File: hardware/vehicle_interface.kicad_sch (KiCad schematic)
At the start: 25 parts, among them IC6 MCP3202-CI_SN, IC7 MCP251863T-E_9PX, J2 FCR7350B, J3 FCR7350G, J4 FCR7350Y, Y2 Crystal_GND24

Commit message: Schematic and PCB layout near final
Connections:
- net +3.3VA renamed +3V3
- net CAN_INT1_ISO renamed CAN_INT1
- net CAN_INT_ISO renamed CAN_INT
- net SPI0_CS_ISO renamed SPI0_CS
- net SPI0_RX_ISO renamed SPI0_RX
- net SPI0_SCK_ISO renamed SPI0_SCK
- net SPI0_TX_ISO renamed SPI0_TX
- net SPI1_CS_ISO renamed SPI1_CS
- net SPI1_RX_ISO renamed SPI1_RX
- net SPI1_SCK_ISO renamed SPI1_SCK
- net SPI1_TX_ISO renamed SPI1_TX

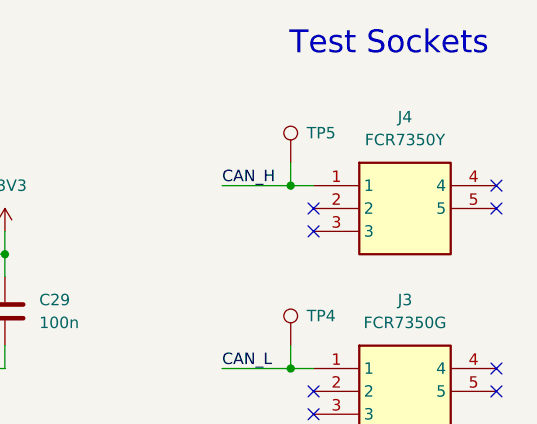
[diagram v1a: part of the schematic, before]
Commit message: Test Terminal Fix
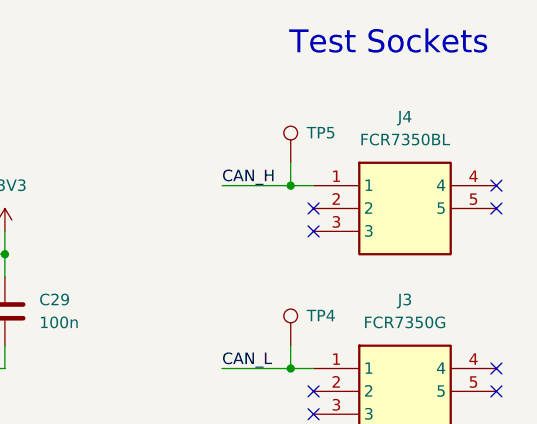
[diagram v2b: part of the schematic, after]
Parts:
- J4: value FCR7350Y -> FCR7350BL
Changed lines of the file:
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@@
 			)
 		)
-		(property "Value" "FCR7350Y"
+		(property "Value" "FCR7350BL"
 			(at 257.81 35.56 0)
 			(show_name no)

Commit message: Schematic Clean Up
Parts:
- D1, D2: JLC Part Number (none) -> C464127
- D3, D4: JLC Part Number (none) -> C83333
- IC6: JLC Part Number (none) -> C56997
- IC7: JLC Part Number (none) -> C20295647
- J2, J3, J4, TP4, TP5, TP8, TP9: now left out of the parts list
- Y2: JLC Part Number (none) -> C6758395
